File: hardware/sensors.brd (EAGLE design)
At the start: 80 x 80 mm, 31 parts, among them U1 DS18B20, U2 DS18B20, U3 DS18B20

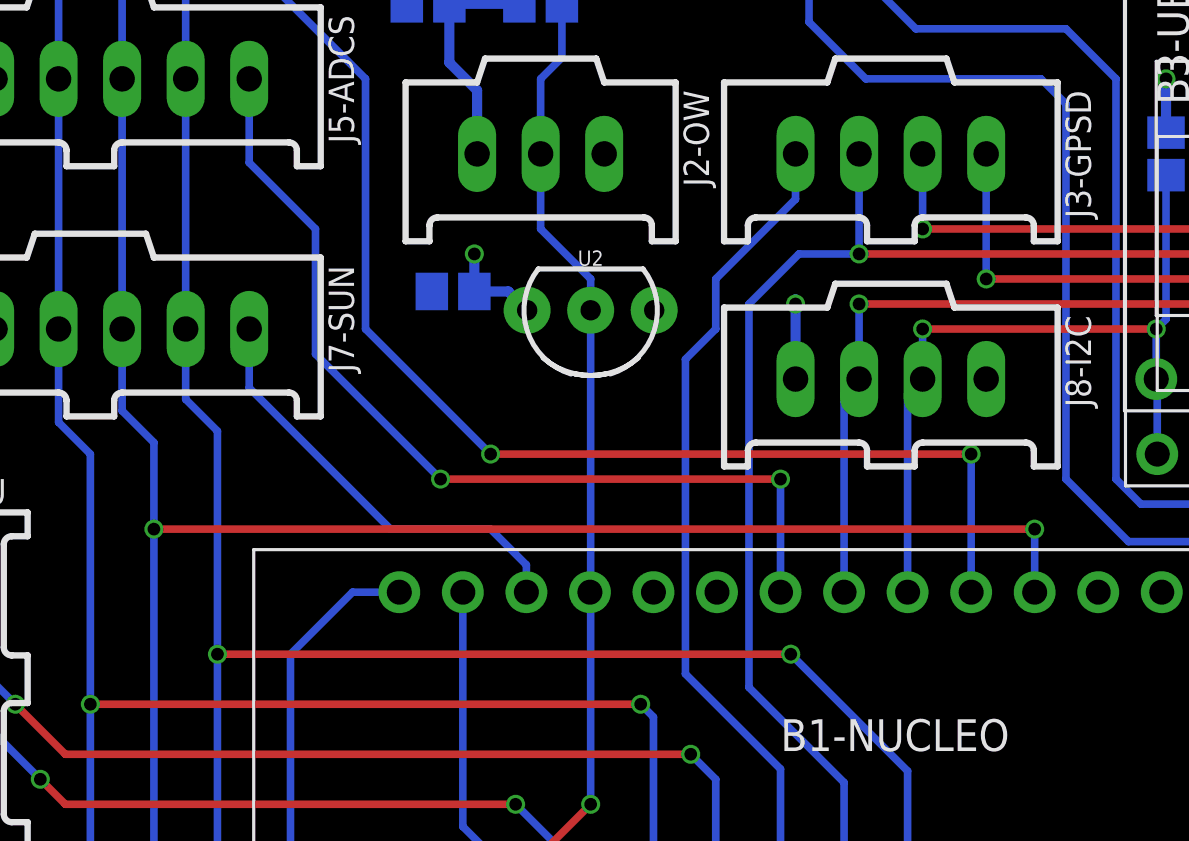
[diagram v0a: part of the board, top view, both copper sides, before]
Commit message: Add cap for I2C connector
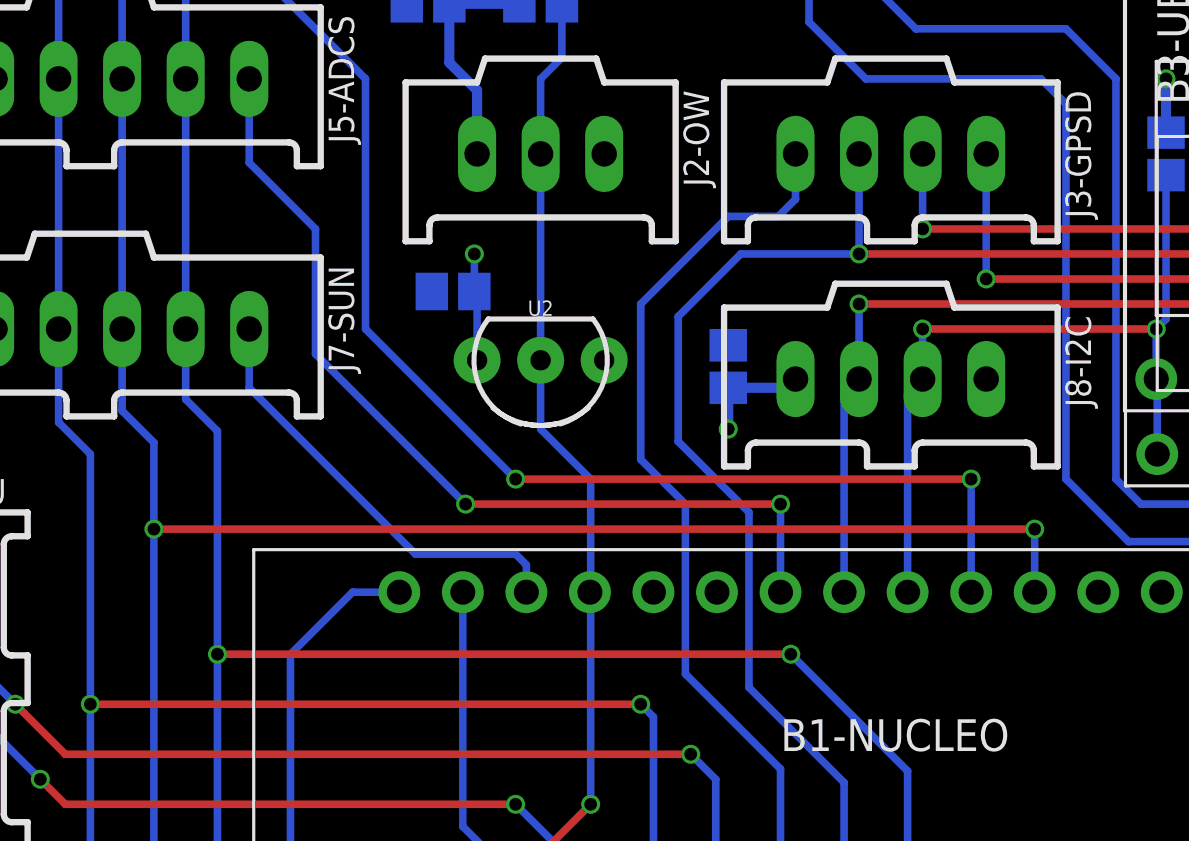
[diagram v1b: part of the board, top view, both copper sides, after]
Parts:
- added C3: 0.1uF, rcl:C2012
- moved U2 2.83 mm to (34.0, 53.8)
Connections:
- net GND: now also C3.1
- net VCC: now also C3.2
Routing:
- net GPS-TP: track 70.7 -> 74.4 mm
- net DBG-TX: track 36.2 -> 38.8 mm
- net VCC: track 90.2 -> 91.9 mm
- net SPI-CS-ENV0: track 53.7 -> 53.1 mm
- net SPI-CS-ADCS: track 37.3 -> 36.7 mm
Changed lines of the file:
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@@
 <setting verticaltext="up"/>
 </settings>
-<grid distance="1" unitdist="mm" unit="mm" style="lines" multiple="1" display="yes" altdistance="0.1" altunitdist="mm" altunit="mm"/>
+<grid distance="1" unitdist="mm" unit="mm" style="lines" multiple="1" display="yes" altdistance="0.5" altunitdist="mm" altunit="mm"/>
 <layers>
 <layer number="1" name="Top" color="4" fill="1" visible="yes" active="yes"/>
@@
 <wire x1="11.7" y1="38.1" x2="11.7" y2="36.2" width="0.1016" layer="41"/>
 <wire x1="11.7" y1="36.2" x2="8.3" y2="36.2" width="0.1016" layer="41"/>
-<circle x="33.45" y="55.75" radius="1.097721875" width="0.1016" layer="41"/>
+<circle x="31.45" y="53.75" radius="1.097721875" width="0.1016" layer="41"/>
 <circle x="30.45" y="74" radius="1.097721875" width="0.1016" layer="41"/>
 <circle x="8.45" y="30" radius="1.097721875" width="0.1016" layer="41"/>
@@
 <attribute name="STORE_ID" value="SEN-00245" x="11" y="30" size="1.778" layer="27" rot="R180" display="off"/>
 </element>
-<element name="U2" library="Frcy" package="TO-92-AMMO" value="DS18B20" x="36" y="55.75" rot="R180">
-<attribute name="STORE_ID" value="SEN-00245" x="36" y="55.75" size="1.778" layer="27" rot="R180" display="off"/>
+<element name="U2" library="Frcy" package="TO-92-AMMO" value="DS18B20" x="34" y="53.75" rot="R180">
+<attribute name="STORE_ID" value="SEN-00245" x="34" y="53.75" size="1.778" layer="27" rot="R180" display="off"/>
 </element>
 <element name="R2" library="rcl" library_urn="urn:adsk.eagle:library:334" package="R2012" package3d_urn="urn:adsk.eagle:package:23543/2" value="10k" x="60" y="33" rot="MR0">
@@
 <element name="B7-UBLOXE" library="Frcy" package="UPUTRONICS-UBLOX-M8Q" value="" x="67.5" y="53"/>
 <element name="J8-I2C" library="con-molex-c-grid" package="90136-1?04" value="" x="48" y="53" rot="R180"/>
+<element name="C3" library="rcl" library_urn="urn:adsk.eagle:library:334" package="C2012" package3d_urn="urn:adsk.eagle:package:23625/2" value="0.1uF" x="41.5" y="53.5" rot="MR270">
+<attribute name="SPICEPREFIX" value="C" x="41.5" y="53.5" size="1.778" layer="28" rot="MR270" display="off"/>
+</element>
 </elements>
 <signals>
@@
 <via x="71.35" y="48" extent="1-16" drill="0.508"/>
 <contactref element="J8-I2C" pad="4"/>
-<wire x1="33.46" y1="55.75" x2="32.71" y2="56.5" width="0.4064" layer="16"/>
-<wire x1="32.71" y1="56.5" x2="31.35" y2="56.5" width="0.4064" layer="16"/>
-<wire x1="31.35" y1="56.5" x2="31.35" y2="58" width="0.4064" layer="16"/>
-<wire x1="44.19" y1="53" x2="44.19" y2="56" width="0.4064" layer="16"/>
-<wire x1="44.19" y1="56" x2="44.19" y2="56.19" width="0.4064" layer="16"/>
-<via x="44.19" y="56" extent="1-16" drill="0.508"/>
 <wire x1="62" y1="62.85" x2="62" y2="65" width="0.4064" layer="16"/>
 <wire x1="59" y1="62.85" x2="59" y2="65" width="0.4064" layer="16"/>
 <via x="59" y="65" extent="1-16" drill="0.508"/>
 <via x="62" y="65" extent="1-16" drill="0.508"/>
+<wire x1="31.46" y1="53.75" x2="31.46" y2="56.39" width="0.3048" layer="16"/>
+<wire x1="31.46" y1="56.39" x2="31.35" y2="56.5" width="0.3048" layer="16"/>
+<wire x1="31.35" y1="58" x2="31.35" y2="56.5" width="0.3048" layer="16"/>
+<contactref element="C3" pad="2"/>
+<wire x1="44.19" y1="53" x2="43.84" y2="52.65" width="0.4064" layer="16"/>
+<wire x1="43.84" y1="52.65" x2="41.5" y2="52.65" width="0.4064" layer="16"/>
+<wire x1="41.5" y1="52.65" x2="41.5" y2="51" width="0.4064" layer="16"/>
+<via x="41.5" y="51" extent="1-16" drill="0.508"/>
 </signal>
 <signal name="GND">
@@
 <contactref element="B7-UBLOXE" pad="GND"/>
 <contactref element="J8-I2C" pad="1"/>
+<contactref element="C3" pad="1"/>
 </signal>
 <signal name="IMU-SDA">
@@
 <wire x1="53.75" y1="44.48" x2="53.75" y2="47" width="0.3048" layer="16"/>
 <via x="53.75" y="47" extent="1-16" drill="0.508"/>
-<wire x1="18.54" y1="47" x2="53.75" y2="47" width="0.3048" layer="1"/>
+<wire x1="18.54" y1="47" x2="28" y2="47" width="0.3048" layer="1"/>
+<wire x1="28" y1="47" x2="53.75" y2="47" width="0.3048" layer="1"/>
 </signal>
 <signal name="SPI-CS-ADCS">
 <contactref element="B1-NUCLEO" pad="D6"/>
 <contactref element="J5-ADCS" pad="1"/>
-<via x="30" y="49" extent="1-16" drill="0.508"/>
-<wire x1="30" y1="49" x2="25" y2="54" width="0.3048" layer="16"/>
+<via x="31" y="48" extent="1-16" drill="0.508"/>
+<wire x1="31" y1="48" x2="25" y2="54" width="0.3048" layer="16"/>
 <wire x1="25" y1="54" x2="25" y2="59" width="0.3048" layer="16"/>
 <wire x1="22.35" y1="61.65" x2="22.35" y2="65" width="0.3048" layer="16"/>
 <wire x1="25" y1="59" x2="22.35" y2="61.65" width="0.3048" layer="16"/>
-<wire x1="30" y1="49" x2="43.59" y2="49" width="0.3048" layer="1"/>
-<wire x1="43.59" y1="44.48" x2="43.59" y2="49" width="0.3048" layer="16"/>
-<via x="43.59" y="49" extent="1-16" drill="0.508"/>
+<wire x1="31" y1="48" x2="43.59" y2="48" width="0.3048" layer="1"/>
+<wire x1="43.59" y1="44.48" x2="43.59" y2="48" width="0.3048" layer="16"/>
+<via x="43.59" y="48" extent="1-16" drill="0.508"/>
 </signal>
 <signal name="TEMP-OW">
@@
 <wire x1="34.85" y1="65.85" x2="34" y2="65" width="0.3048" layer="16"/>
 <wire x1="35.97" y1="44.48" x2="36" y2="44.51" width="0.3048" layer="16"/>
-<wire x1="36" y1="44.51" x2="36" y2="55.75" width="0.3048" layer="16"/>
-<wire x1="34" y1="59" x2="34" y2="62" width="0.3048" layer="16"/>
+<wire x1="36" y1="44.51" x2="36" y2="49" width="0.3048" layer="16"/>
 <wire x1="34.85" y1="68" x2="34.85" y2="70.15" width="0.3048" layer="16"/>
 <wire x1="33" y1="72" x2="33" y2="74" width="0.3048" layer="16"/>
@@
 <wire x1="12" y1="32" x2="11" y2="31" width="0.4064" layer="16"/>
 <wire x1="11" y1="31" x2="11" y2="30" width="0.4064" layer="16"/>
-<wire x1="36" y1="55.75" x2="36" y2="57" width="0.3048" layer="16"/>
-<wire x1="36" y1="57" x2="34" y2="59" width="0.3048" layer="16"/>
+<wire x1="36" y1="49" x2="34" y2="51" width="0.3048" layer="16"/>
+<wire x1="34" y1="51" x2="34" y2="53.75" width="0.3048" layer="16"/>
+<wire x1="34" y1="53.75" x2="34" y2="62" width="0.3048" layer="16"/>
 </signal>
 <signal name="SPI-SCK">
@@
 <contactref element="B1-NUCLEO" pad="D3"/>
 <contactref element="J6-ENV" pad="1"/>
-<via x="32" y="50" extent="1-16" drill="0.508"/>
-<wire x1="32" y1="50" x2="27" y2="55" width="0.3048" layer="16"/>
+<via x="33" y="49" extent="1-16" drill="0.508"/>
+<wire x1="33" y1="49" x2="27" y2="55" width="0.3048" layer="16"/>
 <wire x1="27" y1="55" x2="27" y2="65" width="0.3048" layer="16"/>
 <wire x1="22.35" y1="69.65" x2="22.35" y2="75" width="0.3048" layer="16"/>
 <wire x1="27" y1="65" x2="22.35" y2="69.65" width="0.3048" layer="16"/>
-<wire x1="51.21" y1="44.48" x2="51.21" y2="50" width="0.3048" layer="16"/>
-<via x="51.21" y="50" extent="1-16" drill="0.508"/>
-<wire x1="32" y1="50" x2="51.21" y2="50" width="0.3048" layer="1"/>
+<wire x1="51.21" y1="44.48" x2="51.21" y2="49" width="0.3048" layer="16"/>
+<via x="51.21" y="49" extent="1-16" drill="0.508"/>
+<wire x1="33" y1="49" x2="51.21" y2="49" width="0.3048" layer="1"/>
 </signal>
 <signal name="DBG-TX">
@@
 <wire x1="43.59" y1="29.24" x2="43.59" y2="37.41" width="0.3048" layer="16"/>
 <wire x1="43.59" y1="37.41" x2="39.788" y2="41.212" width="0.3048" layer="16"/>
-<wire x1="41" y1="55" x2="41" y2="57" width="0.3048" layer="16"/>
-<wire x1="41" y1="57" x2="44.19" y2="60.19" width="0.3048" layer="16"/>
+<wire x1="39.788" y1="41.212" x2="39.788" y2="48" width="0.3048" layer="16"/>
+<wire x1="39.788" y1="48" x2="38" y2="49.788" width="0.3048" layer="16"/>
+<wire x1="38" y1="49.788" x2="38" y2="56" width="0.3048" layer="16"/>
+<wire x1="38" y1="56" x2="41.5" y2="59.5" width="0.3048" layer="16"/>
 <wire x1="44.19" y1="60.19" x2="44.19" y2="62" width="0.3048" layer="16"/>
-<wire x1="39.788" y1="53.788" x2="41" y2="55" width="0.3048" layer="16"/>
-<wire x1="39.788" y1="41.212" x2="39.788" y2="53.788" width="0.3048" layer="16"/>
+<wire x1="41.5" y1="59.5" x2="43.5" y2="59.5" width="0.3048" layer="16"/>
+<wire x1="43.5" y1="59.5" x2="44.19" y2="60.19" width="0.3048" layer="16"/>
 </signal>
 <signal name="VIN">
@@
 <contactref element="B1-NUCLEO" pad="D10"/>
 <contactref element="J7-SUN" pad="1"/>
-<wire x1="33.43" y1="44.48" x2="33.43" y2="45.57" width="0.3048" layer="16"/>
-<wire x1="32" y1="47" x2="28" y2="47" width="0.3048" layer="16"/>
-<wire x1="28" y1="47" x2="22.35" y2="52.65" width="0.3048" layer="16"/>
-<wire x1="22.35" y1="52.65" x2="22.35" y2="55" width="0.3048" layer="16"/>
-<wire x1="33.43" y1="45.57" x2="32" y2="47" width="0.3048" layer="16"/>
+<wire x1="22.35" y1="55" x2="22.35" y2="52.65" width="0.3048" layer="16"/>
+<wire x1="33" y1="46" x2="33.43" y2="45.57" width="0.3048" layer="16"/>
+<wire x1="33.43" y1="45.57" x2="33.43" y2="44.48" width="0.3048" layer="16"/>
+<wire x1="22.35" y1="52.65" x2="29" y2="46" width="0.3048" layer="16"/>
+<wire x1="29" y1="46" x2="33" y2="46" width="0.3048" layer="16"/>
 </signal>
 <signal name="SUN-RX">
@@
 <wire x1="71.31" y1="53" x2="71.31" y2="55.46" width="0.3048" layer="16"/>
 <wire x1="71.31" y1="55.46" x2="68.77" y2="58" width="0.3048" layer="16"/>
-<wire x1="42.328" y1="56" x2="42.328" y2="40.672" width="0.3048" layer="16"/>
-<wire x1="46.73" y1="58" x2="44.328" y2="58" width="0.3048" layer="16"/>
-<wire x1="44.328" y1="58" x2="42.328" y2="56" width="0.3048" layer="16"/>
+<wire x1="46.73" y1="58" x2="42" y2="58" width="0.3048" layer="16"/>
+<wire x1="42.328" y1="40.672" x2="42.328" y2="47.672" width="0.3048" layer="16"/>
+<wire x1="39.5" y1="55.5" x2="39.5" y2="50.5" width="0.3048" layer="16"/>
+<wire x1="39.5" y1="50.5" x2="42.328" y2="47.672" width="0.3048" layer="16"/>
+<wire x1="42" y1="58" x2="39.5" y2="55.5" width="0.3048" layer="16"/>
 </signal>
 </signals>

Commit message: Add some labels
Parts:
- moved C10 0.50 mm to (27.0, 73.5)
- moved C9 0.50 mm to (30.5, 57.0)
- moved U3 0.50 mm to (33.0, 73.5)
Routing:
- net VCC: track 91.9 -> 92.4 mm, vias 20 -> 21
- net TEMP-OW: track 68.0 -> 67.5 mm
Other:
- board text added: "GND"
- board text added: "VCC"
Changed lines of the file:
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@@
 <wire x1="11.7" y1="36.2" x2="8.3" y2="36.2" width="0.1016" layer="41"/>
 <circle x="31.45" y="53.75" radius="1.097721875" width="0.1016" layer="41"/>
-<circle x="30.45" y="74" radius="1.097721875" width="0.1016" layer="41"/>
+<circle x="30.45" y="73.5" radius="1.097721875" width="0.1016" layer="41"/>
 <circle x="8.45" y="30" radius="1.097721875" width="0.1016" layer="41"/>
 <hole x="24" y="7.5" drill="2"/>
@@
 <wire x1="45.2" y1="51.3" x2="43.2" y2="51.3" width="0.1016" layer="41"/>
 <wire x1="43.2" y1="51.3" x2="43.2" y2="54.7" width="0.1016" layer="41"/>
+<text x="29.5" y="76" size="0.8128" layer="25" rot="R180" align="top-right">VCC</text>
+<text x="32.5" y="78" size="0.8128" layer="25" rot="R180">GND</text>
 </plain>
 <attributes>
@@
 <element name="J5-ADCS" library="con-molex-c-grid" package="90136-1?06" value="" x="16" y="65" rot="R180"/>
 <element name="J7-SUN" library="con-molex-c-grid" package="90136-1?06" value="" x="16" y="55" rot="R180"/>
-<element name="U3" library="Frcy" package="TO-92-AMMO" value="DS18B20" x="33" y="74" rot="R180">
-<attribute name="STORE_ID" value="SEN-00245" x="33" y="74" size="1.778" layer="27" rot="R180" display="off"/>
+<element name="U3" library="Frcy" package="TO-92-AMMO" value="DS18B20" x="33" y="73.5" rot="R180">
+<attribute name="STORE_ID" value="SEN-00245" x="33" y="73.5" size="1.778" layer="27" rot="R180" display="off"/>
 </element>
 <element name="R5" library="rcl" library_urn="urn:adsk.eagle:library:334" package="R2012" package3d_urn="urn:adsk.eagle:package:23543/2" value="4.7k" x="62" y="62" rot="MR270">
@@
 <attribute name="SPICEPREFIX" value="C" x="7" y="27" size="1.778" layer="28" rot="MR180" display="off"/>
 </element>
-<element name="C9" library="rcl" library_urn="urn:adsk.eagle:library:334" package="C2012" package3d_urn="urn:adsk.eagle:package:23625/2" value="0.1uF" x="30.5" y="56.5" rot="MR180">
-<attribute name="SPICEPREFIX" value="C" x="30.5" y="56.5" size="1.778" layer="28" rot="MR180" display="off"/>
-</element>
-<element name="C10" library="rcl" library_urn="urn:adsk.eagle:library:334" package="C2012" package3d_urn="urn:adsk.eagle:package:23625/2" value="0.1uF" x="27" y="74" rot="MR180">
-<attribute name="SPICEPREFIX" value="C" x="27" y="74" size="1.778" layer="28" rot="MR180" display="off"/>
+<element name="C9" library="rcl" library_urn="urn:adsk.eagle:library:334" package="C2012" package3d_urn="urn:adsk.eagle:package:23625/2" value="0.1uF" x="30.5" y="57" rot="MR180">
+<attribute name="SPICEPREFIX" value="C" x="30.5" y="57" size="1.778" layer="28" rot="MR180" display="off"/>
+</element>
+<element name="C10" library="rcl" library_urn="urn:adsk.eagle:library:334" package="C2012" package3d_urn="urn:adsk.eagle:package:23625/2" value="0.1uF" x="27" y="73.5" rot="MR180">
+<attribute name="SPICEPREFIX" value="C" x="27" y="73.5" size="1.778" layer="28" rot="MR180" display="off"/>
 </element>
 <element name="B6-BLE" library="Frcy" package="HUAMAO-HM-11" value="" x="57" y="14" rot="R270"/>
@@
 <contactref element="R1" pad="2"/>
 <wire x1="30.35" y1="68" x2="33.15" y2="68" width="0.4064" layer="16"/>
-<via x="31.35" y="58" extent="1-16" drill="0.508"/>
-<wire x1="30.46" y1="74" x2="27.85" y2="74" width="0.4064" layer="16"/>
-<wire x1="27.85" y1="74" x2="28" y2="73.85" width="0.4064" layer="16"/>
-<wire x1="28" y1="73.85" x2="28" y2="72" width="0.4064" layer="16"/>
-<via x="28" y="72" extent="1-16" drill="0.508"/>
+<via x="31.35" y="58.5" extent="1-16" drill="0.508"/>
+<wire x1="30.46" y1="73.5" x2="27.85" y2="73.5" width="0.4064" layer="16"/>
+<wire x1="27.85" y1="73.5" x2="28" y2="73.35" width="0.4064" layer="16"/>
+<wire x1="28" y1="73.35" x2="28" y2="71.5" width="0.4064" layer="16"/>
+<via x="28" y="71.5" extent="1-16" drill="0.508"/>
 <wire x1="7.85" y1="27" x2="10" y2="27" width="0.4064" layer="16"/>
 <via x="10" y="27" extent="1-16" drill="0.508"/>
@@
 <via x="59" y="65" extent="1-16" drill="0.508"/>
 <via x="62" y="65" extent="1-16" drill="0.508"/>
-<wire x1="31.46" y1="53.75" x2="31.46" y2="56.39" width="0.3048" layer="16"/>
-<wire x1="31.46" y1="56.39" x2="31.35" y2="56.5" width="0.3048" layer="16"/>
-<wire x1="31.35" y1="58" x2="31.35" y2="56.5" width="0.3048" layer="16"/>
+<wire x1="31.46" y1="53.75" x2="31.46" y2="56.89" width="0.3048" layer="16"/>
+<wire x1="31.46" y1="56.89" x2="31.35" y2="57" width="0.3048" layer="16"/>
+<wire x1="31.35" y1="58.5" x2="31.35" y2="57" width="0.3048" layer="16"/>
 <contactref element="C3" pad="2"/>
 <wire x1="44.19" y1="53" x2="43.84" y2="52.65" width="0.4064" layer="16"/>
@@
 <wire x1="41.5" y1="52.65" x2="41.5" y2="51" width="0.4064" layer="16"/>
 <via x="41.5" y="51" extent="1-16" drill="0.508"/>
+<via x="28" y="77" extent="1-16" drill="1.524"/>
 </signal>
 <signal name="GND">
@@
 <vertex x="1" y="1"/>
 </polygon>
-<via x="35" y="77" extent="1-16" drill="1.524"/>
+<via x="34" y="77" extent="1-16" drill="1.524"/>
 <contactref element="U1" pad="1"/>
 <contactref element="C8" pad="1"/>
@@
 <wire x1="35.97" y1="44.48" x2="36" y2="44.51" width="0.3048" layer="16"/>
 <wire x1="36" y1="44.51" x2="36" y2="49" width="0.3048" layer="16"/>
-<wire x1="34.85" y1="68" x2="34.85" y2="70.15" width="0.3048" layer="16"/>
-<wire x1="33" y1="72" x2="33" y2="74" width="0.3048" layer="16"/>
-<wire x1="34.85" y1="70.15" x2="33" y2="72" width="0.3048" layer="16"/>
+<wire x1="33" y1="73.5" x2="33" y2="71.5" width="0.3048" layer="16"/>
 <wire x1="12" y1="32" x2="11" y2="31" width="0.4064" layer="16"/>
 <wire x1="11" y1="31" x2="11" y2="30" width="0.4064" layer="16"/>
@@
 <wire x1="34" y1="51" x2="34" y2="53.75" width="0.3048" layer="16"/>
 <wire x1="34" y1="53.75" x2="34" y2="62" width="0.3048" layer="16"/>
+<wire x1="33" y1="71.5" x2="34.85" y2="69.65" width="0.3048" layer="16"/>
+<wire x1="34.85" y1="69.65" x2="34.85" y2="68" width="0.3048" layer="16"/>
 </signal>
 <signal name="SPI-SCK">
